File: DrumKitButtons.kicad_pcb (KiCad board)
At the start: 2 copper layers, 124.5 x 43.8 mm, 25 parts, among them J1 Input, J2 Output, U1 74HC165, U2 TLC5916

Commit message: next revision
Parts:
- R9: value 250R -> 400R
- SW1, SW2, SW3, SW4, SW5, SW6, SW7, SW8: moved to B.Cu
- turned SW1 to 180 degrees
- turned SW2 to 180 degrees
- turned SW3 to 180 degrees
- turned SW4 to 180 degrees
- turned SW5 to 180 degrees
- turned SW6 to 180 degrees
- turned SW7 to 180 degrees
- turned SW8 to 180 degrees
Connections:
- SW1 pad 5: /LED_{1} -> VCC
- SW1 pad 6: GND -> /LED_{1}
- SW2 pad 5: /LED_{2} -> VCC
- SW2 pad 6: GND -> /LED_{2}
- SW3 pad 5: /LED_{3} -> VCC
- SW3 pad 6: GND -> /LED_{3}
- SW4 pad 5: /LED_{4} -> VCC
- SW4 pad 6: GND -> /LED_{4}
- SW5 pad 5: /LED_{5} -> VCC
- SW5 pad 6: GND -> /LED_{5}
- SW6 pad 5: /LED_{6} -> VCC
- SW6 pad 6: GND -> /LED_{6}
- SW7 pad 5: /LED_{7} -> VCC
- SW7 pad 6: GND -> /LED_{7}
- SW8 pad 5: /LED_{8} -> VCC
- SW8 pad 6: GND -> /LED_{8}
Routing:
- net /DI_{LED}: track 73.9 -> 181.6 mm, vias 4 -> 0
- net /DI_{SW}: track 52.7 -> 125.7 mm, vias 3 -> 1
- net VCC: track 185.2 -> 239.6 mm, vias 4 -> 1
- net /SW_{8}: track 56.5 -> 64.2 mm
- net /SW_{7}: track 43.4 -> 51.1 mm
- net /SW_{6}: track 30.3 -> 37.9 mm
- net /SW_{1}: track 62.7 -> 55.1 mm
- net /SW_{2}: track 44.2 -> 38.1 mm
- net /CLK_{LED}: track 112.1 -> 106.1 mm
- net /DO_{SW}: track 49.2 -> 53.8 mm, vias 0 -> 2
- net /~{PL_{SW}}: track 88.4 -> 84.2 mm, vias 1 -> 0
- net /SW_{3}: track 25.6 -> 22.4 mm
- net /LE_{LED}: track 110.1 -> 108.3 mm
- net /CLK_{SW}: track 91.5 -> 90.1 mm, vias 1 -> 0
- net /~{OE_{LED}}: track 108.6 -> 109.5 mm
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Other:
- board size 124.5 x 43.8 mm -> 124.3 x 42.7 mm

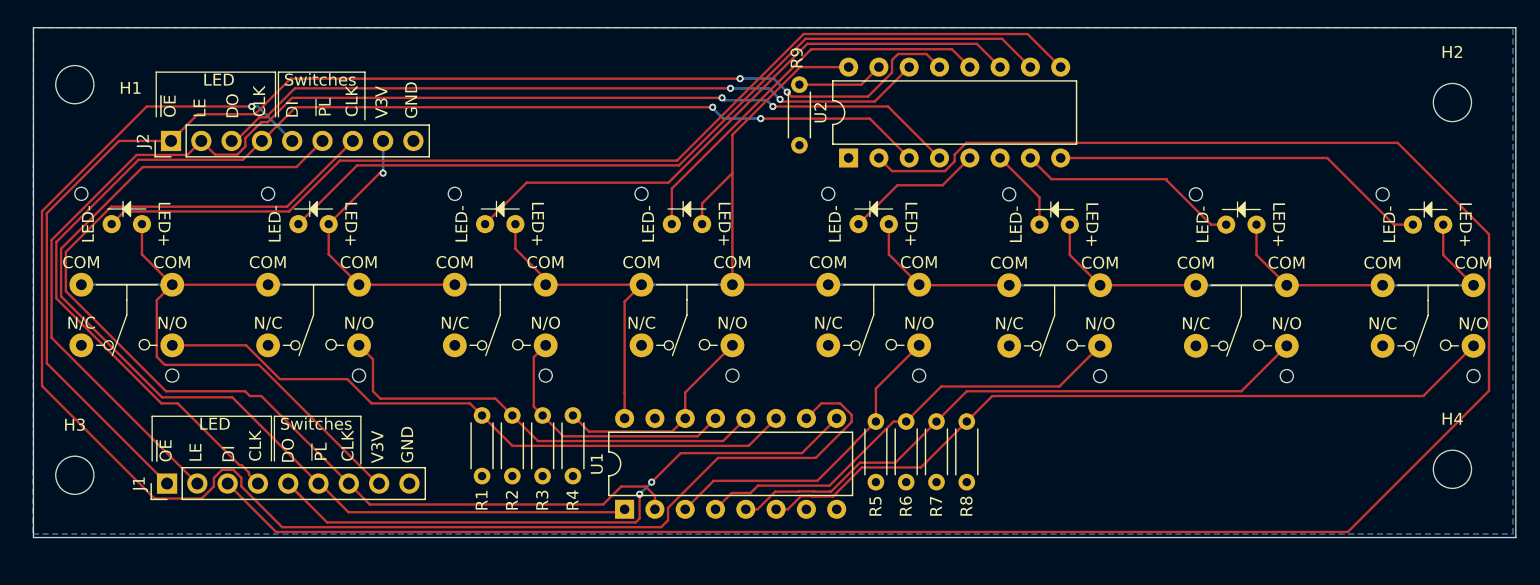
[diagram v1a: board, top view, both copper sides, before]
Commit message: clean up traces; make VCC zone
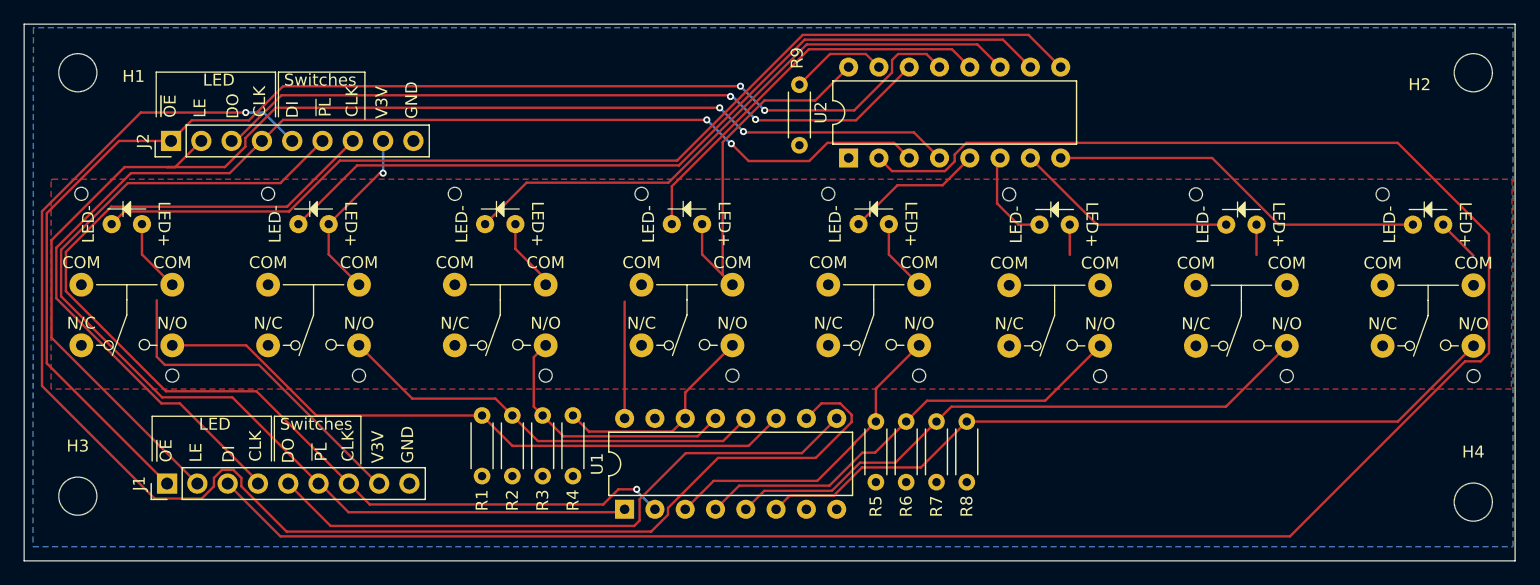
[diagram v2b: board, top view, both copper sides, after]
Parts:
- moved H4 3.26 mm to (171.5, 86.0)
- moved H2 3.05 mm to (171.5, 50.0)
- moved H3 1.77 mm to (54.5, 85.5)
- moved H1 1.03 mm to (54.5, 50.0)
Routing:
- net VCC: track 239.6 -> 109.7 mm
- net /LE_{LED}: track 108.3 -> 110.5 mm
- net /SW_{2}: track 38.1 -> 36.5 mm
- net /DI_{LED}: track 181.6 -> 180.0 mm
- net /DO_{SW}: track 53.8 -> 52.2 mm, vias 2 -> 0
- net Net-(U2-R-EXT): track 7.27 -> 8.19 mm
- net /LED_{6}: track 6.96 -> 7.85 mm
- net /DO_{LED}: track 59.9 -> 60.8 mm
- net /CLK_{SW}: track 90.1 -> 89.3 mm, vias 0 -> 1
- added copper zone on F.Cu, net VCC
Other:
- board size 124.3 x 42.7 mm -> 125 x 45 mm

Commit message: add URL; add extra dimension
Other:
- board text added: "https://github.com/aseanwatson/ DrumKitButtons/releases/tag/v1"
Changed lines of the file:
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@@
+		)
+	)
+	(gr_text "https://github.com/aseanwatson/\n    DrumKitButtons/releases/tag/v1"
+		(at 131.359 83.928 0)
+		(layer "F.SilkS")
+		(effects
+			(font
+				(size 1.3 1.3)
+				(thickness 0.3)
+				(bold yes)
+			)
+			(justify left bottom)
 		)
 	)
@@
 	)
 	(dimension
+		(type aligned)
+		(layer "Dwgs.User")
+		(pts
+			(xy 175 45.928) (xy 175 90.928)
+		)
+		(height -8.359)
+		(gr_text "45.0000 mm"
+			(at 181.559 68.428 90)
+			(layer "Dwgs.User")
+			(effects
+				(font
+					(size 1.5 1.5)
+					(thickness 0.3)
+				)
+			)
+		)
+		(format
+			(prefix "")
+			(suffix "")
+			(units 3)
+			(units_format 1)
+			(precision 4)
+		)
+		(style
+			(thickness 0.2)
+			(arrow_length 1.27)
+			(text_position_mode 0)
+			(extension_height 0.58642)
+			(extension_offset 0.5) keep_text_aligned)
+	)
+	(dimension

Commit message: 2 banks of 8 buttons; ICs on left
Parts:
- added R10: 400R, Resistor_THT:R_Axial_DIN0204_L3.6mm_D1.6mm_P5.08mm_Horizontal, F.Cu at (235.3, 90.6)
- added R11: 47R, Resistor_THT:R_Axial_DIN0204_L3.6mm_D1.6mm_P5.08mm_Horizontal, F.Cu at (250.2, 90.6)
- added R12: 47R, Resistor_THT:R_Axial_DIN0204_L3.6mm_D1.6mm_P5.08mm_Horizontal, F.Cu at (265.2, 90.6)
- added R13: 47R, Resistor_THT:R_Axial_DIN0204_L3.6mm_D1.6mm_P5.08mm_Horizontal, F.Cu at (280.3, 90.7)
- added R14: 47R, Resistor_THT:R_Axial_DIN0204_L3.6mm_D1.6mm_P5.08mm_Horizontal, F.Cu at (295.0, 90.6)
- added R15: 47R, Resistor_THT:R_Axial_DIN0204_L3.6mm_D1.6mm_P5.08mm_Horizontal, F.Cu at (310.3, 90.7)
- added R16: 47R, Resistor_THT:R_Axial_DIN0204_L3.6mm_D1.6mm_P5.08mm_Horizontal, F.Cu at (325.3, 90.7)
- added R17: 47R, Resistor_THT:R_Axial_DIN0204_L3.6mm_D1.6mm_P5.08mm_Horizontal, F.Cu at (339.9, 90.7)
- added R18: 47R, Resistor_THT:R_Axial_DIN0204_L3.6mm_D1.6mm_P5.08mm_Horizontal, F.Cu at (355.1, 90.7)
- added SW10: ~, Local:PB86, B.Cu at (235.8, 81.0)
- added SW11: ~, Local:PB86, B.Cu at (190.8, 81.0)
- added SW12: ~, Local:PB86, B.Cu at (205.8, 81.0)
- added SW13: ~, Local:PB86, B.Cu at (175.8, 81.0)
- added SW14: ~, Local:PB86, B.Cu at (145.8, 81.0)
- added SW15: ~, Local:PB86, B.Cu at (160.8, 81.0)
- added SW16: ~, Local:PB86, B.Cu at (130.8, 81.0)
- added SW9: ~, Local:PB86, B.Cu at (220.8, 81.0)
- added U3: 74HC165, Package_DIP:DIP-16_W7.62mm, F.Cu at (65.8, 91.3)
- added U4: TLC5916, Package_DIP:DIP-16_W7.62mm, F.Cu at (95.5, 90.2)
- R1: value 47R -> 400R
- R9: value 400R -> 47R
- moved H3 312.1 mm to (366.6, 86.1)
- moved SW1 297.5 mm to (355.8, 81.0)
- moved SW2 251.9 mm to (325.8, 81.0)
- moved SW3 251.3 mm to (340.8, 81.0)
- moved SW4 205.7 mm to (310.8, 81.0)
- moved H4 195.4 mm to (366.6, 75.6)
- moved SW5 175.1 mm to (295.8, 81.0)
- moved SW6 145.0 mm to (280.8, 81.0)
- moved R9 112.2 mm to (219.9, 90.7), turned to 0 degrees
- moved SW7 99.7 mm to (250.8, 81.0)
- moved SW8 99.0 mm to (265.8, 81.0)
- moved R8 77.0 mm to (205.2, 90.7), turned to 0 degrees
- moved H1 75.7 mm to (120.7, 86.7)
- moved R6 67.1 mm to (190.1, 90.7), turned to 0 degrees
- moved H2 57.1 mm to (120.7, 76.1)
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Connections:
- J1 pad 1: /~{OE_{LED}} -> LE_{LED}
- J1 pad 2: /LE_{LED} -> ~{OE_{LED}}
- J1 pad 3: /DI_{LED} -> CLK_{LED}
- J1 pad 4: /CLK_{LED} -> /DI_{LED}
- J1 pad 6: /~{PL_{SW}} -> CLK_{SW}
- J1 pad 7: /CLK_{SW} -> ~{PL_{SW}}
- J2 pad 1: /~{OE_{LED}} -> LE_{LED}
- J2 pad 2: /LE_{LED} -> ~{OE_{LED}}
- J2 pad 3: /DO_{LED} -> CLK_{LED}
- J2 pad 4: /CLK_{LED} -> /DO_{LED}
- J2 pad 6: /~{PL_{SW}} -> CLK_{SW}
- J2 pad 7: /CLK_{SW} -> ~{PL_{SW}}
- R1 pad 1: /SW_{1} -> Net-(U2-R-EXT)
- R2 pad 1: /SW_{2} -> /Button Bank 0/SW_{0}
- R3 pad 1: /SW_{3} -> /Button Bank 0/SW_{4}
- R4 pad 1: /SW_{4} -> /Button Bank 0/SW_{1}
- R5 pad 1: /SW_{5} -> /Button Bank 0/SW_{5}
- R6 pad 1: /SW_{6} -> /Button Bank 0/SW_{2}
- R7 pad 1: /SW_{7} -> /Button Bank 0/SW_{6}
- R8 pad 1: /SW_{8} -> /Button Bank 0/SW_{3}
- R9 pad 1: Net-(U2-R-EXT) -> /Button Bank 0/SW_{7}
- SW1 pad 2: /SW_{1} -> /Button Bank 0/SW_{0}
- SW1 pad 6: /LED_{1} -> /Button Bank 0/LED_{0}
- SW2 pad 2: /SW_{2} -> /Button Bank 0/SW_{4}
- SW2 pad 6: /LED_{2} -> /Button Bank 0/LED_{4}
- SW3 pad 2: /SW_{3} -> /Button Bank 0/SW_{1}
- SW3 pad 6: /LED_{3} -> /Button Bank 0/LED_{1}
- SW4 pad 2: /SW_{4} -> /Button Bank 0/SW_{5}
- SW4 pad 6: /LED_{4} -> /Button Bank 0/LED_{5}
- SW5 pad 2: /SW_{5} -> /Button Bank 0/SW_{2}
- SW5 pad 6: /LED_{5} -> /Button Bank 0/LED_{2}
- SW6 pad 2: /SW_{6} -> /Button Bank 0/SW_{6}
- SW6 pad 6: /LED_{6} -> /Button Bank 0/LED_{6}
- SW7 pad 2: /SW_{7} -> /Button Bank 0/SW_{3}
- SW7 pad 6: /LED_{7} -> /Button Bank 0/LED_{3}
- SW8 pad 2: /SW_{8} -> /Button Bank 0/SW_{7}
- SW8 pad 6: /LED_{8} -> /Button Bank 0/LED_{7}
- U1 pad 1: /~{PL_{SW}} -> ~{PL_{SW}}
- U1 pad 10: /DI_{SW} -> /Button Bank 0/DI_{SW}
- U1 pad 11: /SW_{1} -> /Button Bank 0/SW_{3}
- U1 pad 12: /SW_{2} -> /Button Bank 0/SW_{2}
- U1 pad 13: /SW_{3} -> /Button Bank 0/SW_{1}
- U1 pad 14: /SW_{4} -> /Button Bank 0/SW_{0}
- U1 pad 2: /CLK_{SW} -> CLK_{SW}
- U1 pad 3: /SW_{5} -> /Button Bank 0/SW_{7}
- U1 pad 4: /SW_{6} -> /Button Bank 0/SW_{6}
- U1 pad 5: /SW_{7} -> /Button Bank 0/SW_{5}
- U1 pad 6: /SW_{8} -> /Button Bank 0/SW_{4}
- U2 pad 10: /LED_{2} -> /Button Bank 0/LED_{5}
- U2 pad 11: /LED_{3} -> /Button Bank 0/LED_{6}
- U2 pad 12: /LED_{4} -> /Button Bank 0/LED_{7}
- U2 pad 13: /~{OE_{LED}} -> ~{OE_{LED}}
- U2 pad 14: /DO_{LED} -> /Button Bank 0/DO_{LED}
- U2 pad 3: /CLK_{LED} -> CLK_{LED}
- U2 pad 4: /LE_{LED} -> LE_{LED}
- U2 pad 5: /LED_{5} -> /Button Bank 0/LED_{0}
- U2 pad 6: /LED_{6} -> /Button Bank 0/LED_{1}
- U2 pad 7: /LED_{7} -> /Button Bank 0/LED_{2}
- U2 pad 8: /LED_{8} -> /Button Bank 0/LED_{3}
- U2 pad 9: /LED_{1} -> /Button Bank 0/LED_{4}
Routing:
- net (no net): track 0.00 -> 690.1 mm
- net VCC: track 109.7 -> 405.0 mm, vias 1 -> 0
- net /Button Bank 1/SW_{5}: track 0.00 -> 286.9 mm
- net /Button Bank 1/SW_{6}: track 0.00 -> 274.1 mm
- net /Button Bank 0/LED_{4}: track 0.00 -> 268.0 mm
- net /Button Bank 1/SW_{7}: track 0.00 -> 261.9 mm
- net /Button Bank 0/LED_{2}: track 0.00 -> 256.8 mm
- net /Button Bank 1/LED_{2}: track 0.00 -> 256.1 mm
- net /Button Bank 1/SW_{1}: track 0.00 -> 235.9 mm
- net /Button Bank 1/LED_{6}: track 0.00 -> 234.1 mm
- net /Button Bank 1/LED_{7}: track 0.00 -> 220.8 mm
- net /Button Bank 1/SW_{2}: track 0.00 -> 218.1 mm
- net /Button Bank 1/SW_{3}: track 0.00 -> 200.6 mm
- net /Button Bank 0/LED_{3}: track 0.00 -> 183.3 mm
- net /Button Bank 1/SW_{4}: track 0.00 -> 182.8 mm
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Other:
- board size 125 x 45 mm -> 318 x 28 mm
- board text added: "0"
- board text added: "1"
- board text added: "10"
- board text added: "11"
- board text added: "12"
- board text added: "13"
- board text added: "14"
- board text added: "15"
- board text added: "2"
- board text added: "3"
- board text added: "3V3"
- board text added: "4"
- board text added: "5"
- board text added: "6"
- board text added: "7"
- board text added: "8"
- board text added: "9"
- board text added: "CHAIN"
- board text added: "DATA"
- board text added: "LCH"
- board text added: "MCU"
- board text added: "SWITCH"
- board text added: "https://github.com/aseanwatson/DrumKitButtons/releases/tag/v2"
- board text added: "~{LCH}"
- board text removed: "DI"
- board text removed: "DO"
- board text removed: "LE"
- board text removed: "Switches"
- board text removed: "V3V"
- board text removed: "https://github.com/aseanwatson/ DrumKitButtons/releases/tag/v1"
- board text removed: "~{PL}"
